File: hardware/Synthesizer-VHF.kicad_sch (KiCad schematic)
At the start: 85 parts, among them J1 Screw_Terminal_01x02, J2 Scope, J4 USB-C 2.0 16P, J5 REF_IN, J6 Scope, J7 RFOUTA, J8 Header 1x3, J9 RFOUTB, U1 LM7805A, U2 FT231XQ, U3 ATtiny1616-M, U4 ADF4351, U7 ADP150AUJZ-3.3-R7, U8 ADP150AUJZ-3.3-R7, X1 HCI 8122S-25NQ33FTL

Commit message: Swap J5, J7, and J9 to the Cinch edge-launch SMA
Add a 142-0701-801 land pattern for a 1.57 mm board and place it on
the three connectors without moving them or touching the traces.

Co-authored-by: Jeffrey Millar <wa1hco@users.noreply.github.com>
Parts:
- J5, J7, J9: footprint Synthesizer:SMA_Amphenol_901-143_Horizontal -> Synthesizer:SMA_Cinch_142-0701-801_EdgeMount; LCSC C496551 -> (none); MPN (none) -> 142-0701-801
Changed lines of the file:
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@@
 			)
 		)
-		(property "Footprint" "Synthesizer:SMA_Amphenol_901-143_Horizontal"
+		(property "Footprint" "Synthesizer:SMA_Cinch_142-0701-801_EdgeMount"
 			(at 381 123.19 0)
 			(effects
@@
 			)
 		)
-		(property "Datasheet" "~"
+		(property "Datasheet" "https://www.cinch.com/products/rf-microwave/connectors/142-0701-801"
 			(at 381 123.19 0)
 			(effects
@@
 			)
 		)
-		(property "LCSC" "C496551"
+		(property "MPN" "142-0701-801"
+			(at 381 123.19 0)
+			(effects
+				(font
+					(size 1.27 1.27)
+				)
+				(hide yes)
+			)
+		)
+		(property "LCSC" ""
 			(at 0 246.38 0)
 			(effects
@@
 			)
 		)
-		(property "Footprint" "Synthesizer:SMA_Amphenol_901-143_Horizontal"
+		(property "Footprint" "Synthesizer:SMA_Cinch_142-0701-801_EdgeMount"
 			(at 167.64 143.51 0)
 			(effects
@@
 			)
 		)
-		(property "Datasheet" "~"
+		(property "Datasheet" "https://www.cinch.com/products/rf-microwave/connectors/142-0701-801"
 			(at 167.64 143.51 0)
 			(effects
@@
 			)
 		)
-		(property "LCSC" "C496551"
+		(property "MPN" "142-0701-801"
+			(at 167.64 143.51 0)
+			(effects
+				(font
+					(size 1.27 1.27)
+				)
+				(hide yes)
+			)
+		)
+		(property "LCSC" ""
 			(at 360.68 287.02 0)
 			(effects
@@
 			)
 		)
-		(property "Footprint" "Synthesizer:SMA_Amphenol_901-143_Horizontal"
+		(property "Footprint" "Synthesizer:SMA_Cinch_142-0701-801_EdgeMount"
 			(at 381 135.89 0)
 			(effects
@@
 			)
 		)
-		(property "Datasheet" "~"
+		(property "Datasheet" "https://www.cinch.com/products/rf-microwave/connectors/142-0701-801"
 			(at 381 135.89 0)
 			(effects
@@
 			)
 		)
-		(property "LCSC" "C496551"
+		(property "MPN" "142-0701-801"
+			(at 381 135.89 0)
+			(effects
+				(font
+					(size 1.27 1.27)
+				)
+				(hide yes)
+			)
+		)
+		(property "LCSC" ""
 			(at 0 271.78 0)
 			(effects

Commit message: WIP: user edits (connector placement)
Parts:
- added C34: 10n, Synthesizer:Cap_0402, symbol Device:C
- added J10: REF_IN, Synthesizer:SMA_Cinch_142-0701-801_EdgeMount, symbol Connector:Conn_Coaxial
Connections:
- net GND: now also J10.2 (Ext)
- new net: C34.2, J10.1 (In)

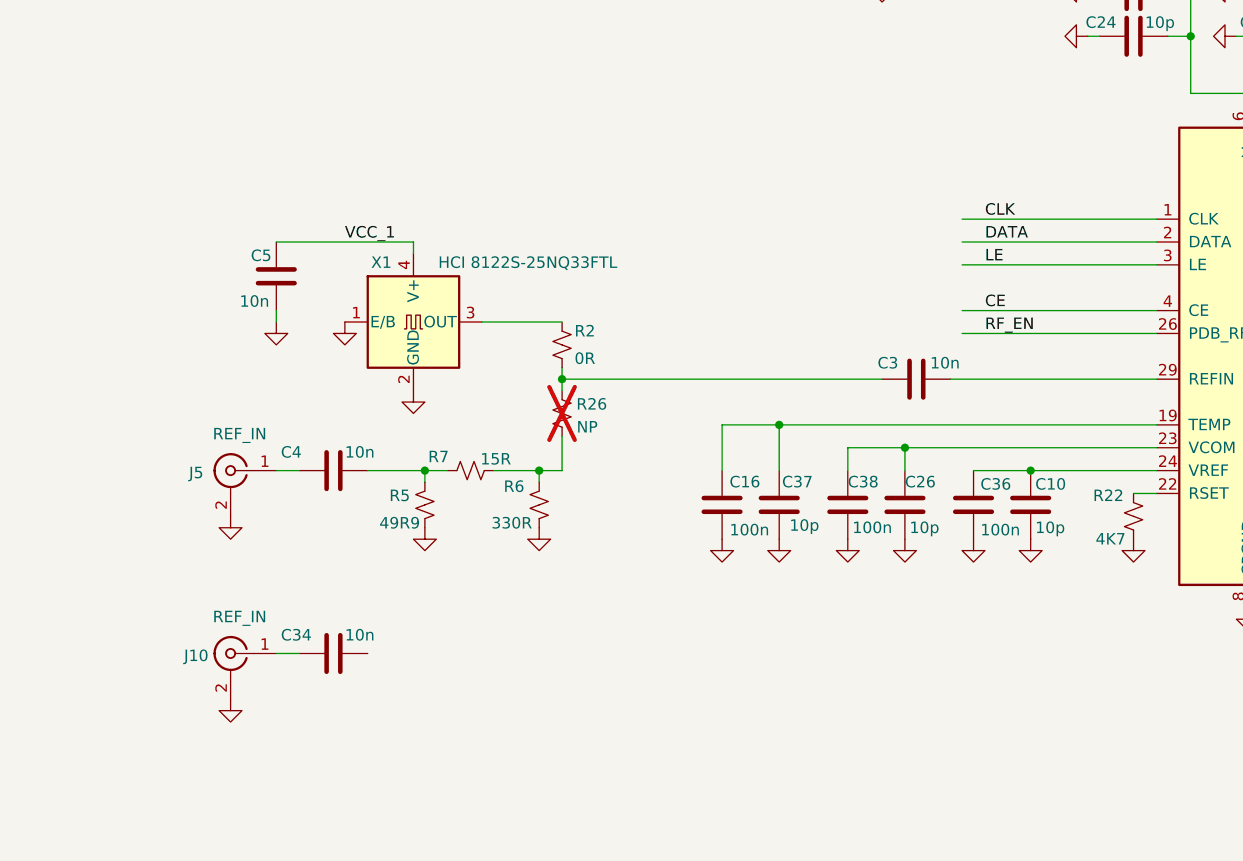
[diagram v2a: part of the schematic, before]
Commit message: Add a buffered reference distribution on the schematic
Square the TCXO with an unbuffered inverter, fan it out to a live
REF OUT and a solder-jumper selection into the ADF4351 REFIN path.

Co-authored-by: Jeffrey Millar <wa1hco@users.noreply.github.com>
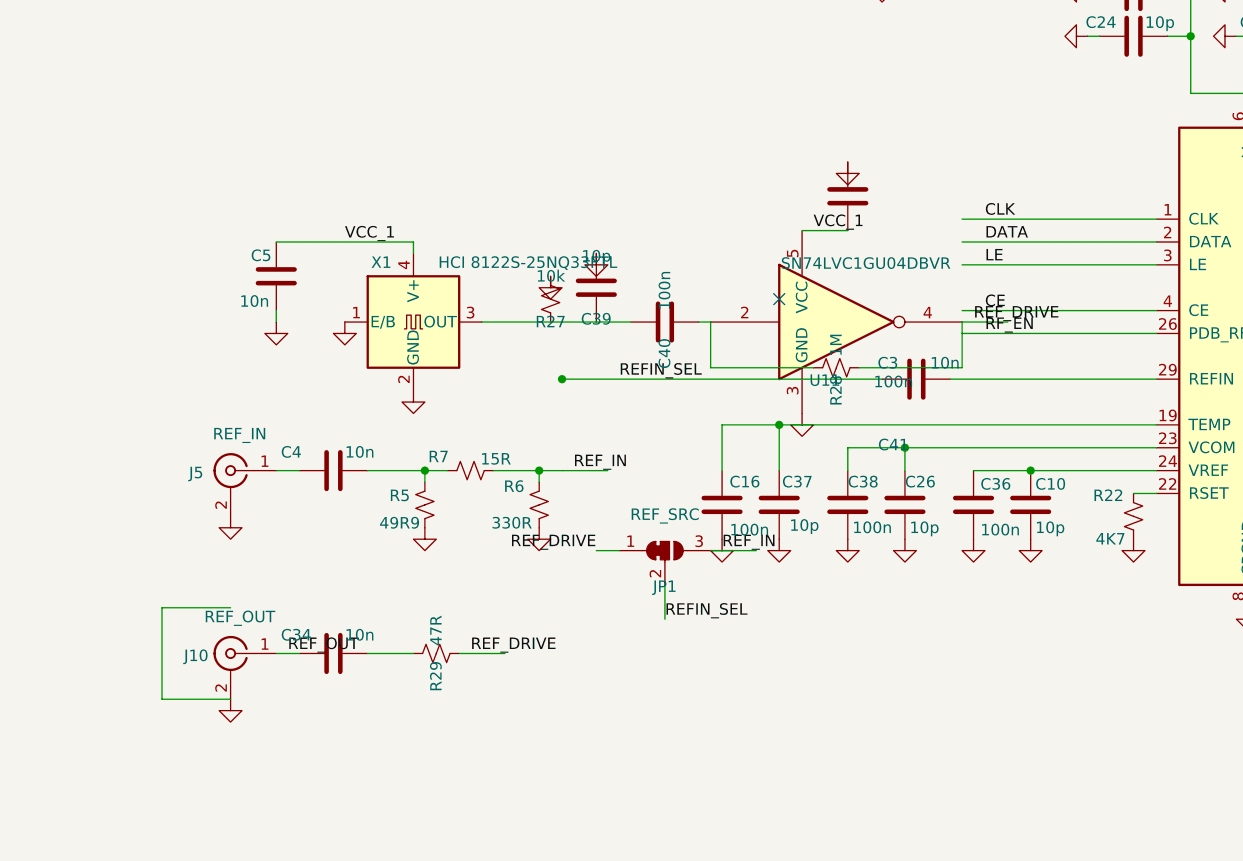
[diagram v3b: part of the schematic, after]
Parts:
- removed R2: 0R, Resistor_SMD:R_0805_2012Metric, symbol Device:R_Small_US
- removed R26: NP, Resistor_SMD:R_0805_2012Metric, symbol Device:R_Small_US
- added C39: 10p, Synthesizer:Cap_0402, symbol Device:C
- added C40, C41: 100n, Synthesizer:Cap_0402, symbol Device:C
- added JP1: REF_SRC, Jumper:SolderJumper-3_P1.3mm_Bridged12_Pad1.0x1.5mm, symbol Jumper:SolderJumper_3_Bridged12
- added R27: 10k, Synthesizer:Res_0402, symbol Device:R_Small_US
- added R28: 1M, Synthesizer:Res_0402, symbol Device:R_Small_US
- added R29: 47R, Synthesizer:Res_0402, symbol Device:R_Small_US
- added U11: SN74LVC1GU04DBVR, Package_TO_SOT_SMD:SOT-23-5, symbol 74xGxx:74LVC1G04
- J10: value REF_IN -> REF_OUT
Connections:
- net GND: now also C39.1, C41.1, R27.1, U11.3 (GND)
- net VCC_1: now also C41.2, U11.5 (VCC)
- net at X1.3 (OUT): now also C39.2, C40.1, R27.2
- net REF_OUT: now reaches C34.2, J10.1 (In)
- net at C34.1: now also R29.1
- net REF_IN: now reaches R6.1, R7.2
- net REF_IN: now also JP1.3 (B)
- net REFIN_SEL: now reaches C3.2
- net REFIN_SEL: now also JP1.2 (C)
- new net: C40.2, R28.1, U11.2
- new net REF_DRIVE: JP1.1 (A), R28.2, R29.2, U11.4
- no-connect marks 14 -> 15

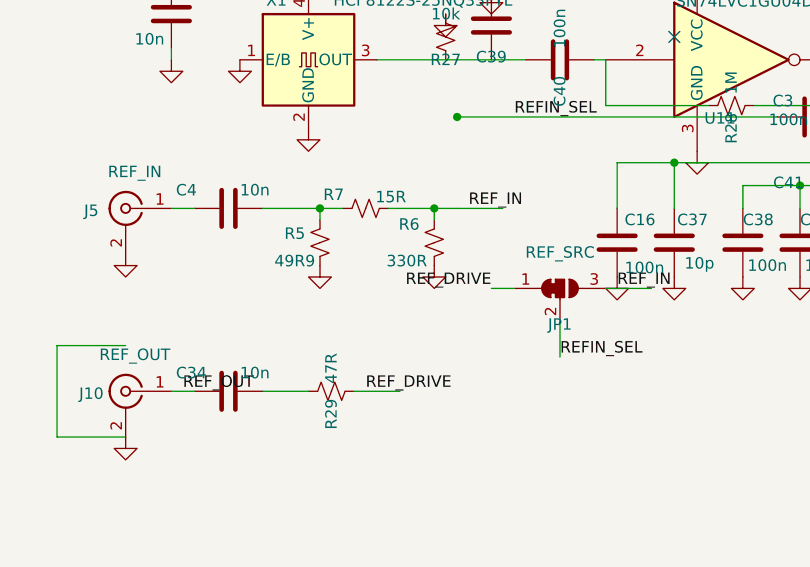
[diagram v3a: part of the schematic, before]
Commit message: Attenuate the local reference into the ADF4351
REF_DRIVE was a 3.3 Vpp square at REFIN, which is the AVDD maximum.
R30 220 ohm in series and R31 510 ohm to ground, between REF_DRIVE and
JP1 pad 1, set that path to about 2.2 Vpp (about 1.7 Vpp if REF OUT is
terminated in 50 ohms) with a few-nanosecond edge at 25 MHz. REF OUT
and REF IN are unchanged. Schematic only.

Co-authored-by: Jeffrey Millar <wa1hco@users.noreply.github.com>
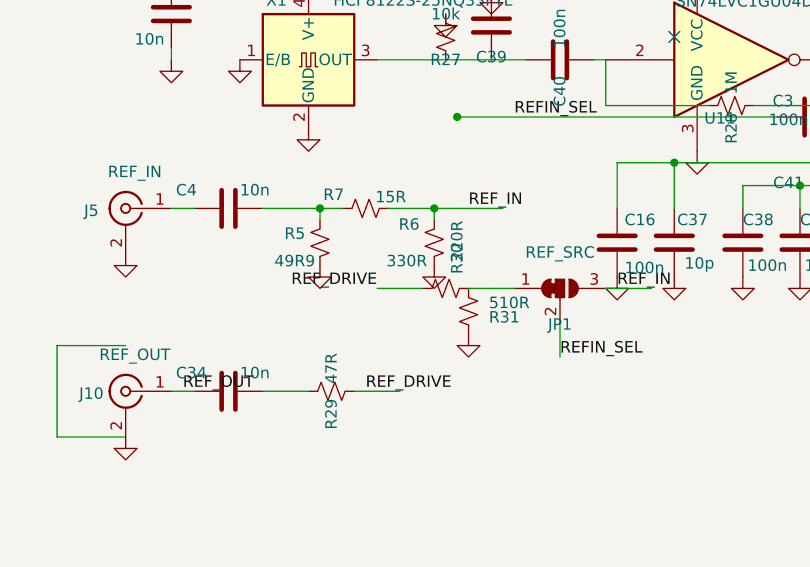
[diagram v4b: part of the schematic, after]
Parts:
- added R30: 220R, Synthesizer:Res_0402, symbol Device:R_Small_US
- added R31: 510R, Synthesizer:Res_0402, symbol Device:R_Small_US
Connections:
- net GND: now also R31.2
- net REF_DRIVE: now also R30.1; no longer JP1.1 (A)
- new net: JP1.1 (A), R30.2, R31.1

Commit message: Extruded enclosure WIP: board edits, rules, footprints (USB-C, SMA), Wurth 20x20 shield footprint, upload port
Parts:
- removed JP1: REF_SRC, Jumper:SolderJumper-3_P1.3mm_Bridged12_Pad1.0x1.5mm, symbol Jumper:SolderJumper_3_Bridged12
- removed R27: 10k, Synthesizer:Res_0402, symbol Device:R_Small_US
- removed U7, U8: ADP150AUJZ-3.3-R7, Package_TO_SOT_SMD:SOT-23-5, symbol Synthesizer:ADP150AUJZ-3.3-R7
- added C35: 1u 10V, Synthesizer:Cap_0402, symbol Device:C
- added C42, C43, C44, C45, C46, C47: 100p, Synthesizer:Cap_0402, symbol Device:C
- added FB2, FB4, FB6: FerriteBead_Small, Inductor_SMD:L_0805_2012Metric, symbol Device:FerriteBead_Small
- added J11: Header 1x3, Connector_PinHeader_2.54mm:PinHeader_1x03_P2.54mm_Vertical, symbol Connector:Conn_01x03_Pin
- added J3: RFShield_TwoPieces, wa1hco:Wurth_WE-SHC_36103205_20x20mm, symbol Device:RFShield_TwoPieces
- added R32: 47R, Synthesizer:Res_0402, symbol Device:R_Small_US
- added U5, U6, U7: LP5907MFX-3.3, Package_TO_SOT_SMD:SOT-23-5, symbol Regulator_Linear:LP5907MFX-3.3
- C39: value 10p -> 1u 10V; LCSC C32949 -> C52923
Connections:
- net 5V: now also C35.1, U5.1 (IN), U5.3 (EN), U6.1 (IN), U6.3 (EN), U7.1 (IN), U7.3 (EN)
- net GND: now also C39.2, C35.2, C42.2, C43.2, C44.2, C45.2, C46.2, C47.2, J3.1 (Shield), U5.2 (GND), U6.2 (GND), U7.2 (GND); no longer C39.1
- net REFIN_SEL: now also R32.2
- net REF_IN: now also J11.3 (Pin_3)
- net VCC_1: no longer C13.1, C18.1, C19.2, C21.2, C24.1, C25.1, C27.1, C28.2, C30.1, U4.10 (AVDD), U4.16 (VVCO), U4.17 (VVCO), U4.28 (DVDD), U4.32 (SDVDD), U4.6 (Vp)
- net at C40.1, X1.3 (OUT): no longer C39.2
- net at R30.2, R31.1: now also J11.1 (Pin_1)
- net REF_DRIVE: no longer names the net of R28.2, R29.2, R30.1, U11.4
- net VCC_2 renamed VRF
- net VRF: now also C43.1, FB2.2; no longer C14.1
- new net: C27.1, C46.1, FB6.1, U7.5 (OUT)
- new net: C39.1, C44.1, FB4.1, U6.5 (OUT)
- new net: C14.1, C42.1, FB2.1, U5.5 (OUT)
- new net: C13.1, C19.2, C21.2, C30.1, U4.28 (DVDD), U4.32 (SDVDD)
- new net: J11.2 (Pin_2), R32.1
- new net VDD: C24.1, C25.1, C47.1, FB6.2, U4.10 (AVDD), U4.6 (Vp)
- new net VVCO: C18.1, C28.2, C45.1, FB4.2, U4.16 (VVCO), U4.17 (VVCO)
- no-connect marks 15 -> 14
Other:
- note added: "Crystal"
- note added: "Ref In"
- note added: "Synth"
- moved on the sheet: C10, C12, C13, C14, C15, C16, C17, C18, C19, C20, C21, C22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
